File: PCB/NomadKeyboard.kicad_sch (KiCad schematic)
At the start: 93 parts, among them J1 4PIN, J2 OLED, P1 i2c_pin, P2 i2c_pin, SW1 SW_PUSH_LED, SW10 SW_PUSH_LED, SW11 SW_PUSH_LED, SW12 SW_PUSH_LED, SW13 SW_PUSH_LED, SW14 SW_PUSH_LED, SW15 SW_PUSH_LED, SW16 SW_PUSH_LED, SW17 SW_PUSH_LED, SW18 SW_PUSH_LED, SW19 SW_PUSH_LED, SW2 SW_PUSH_LED, SW20 SW_PUSH_LED, SW21 SW_PUSH_LED, SW22 SW_PUSH_LED, SW23 SW_PUSH_LED, SW24 SW_PUSH_LED, SW25 SW_PUSH_LED, SW26 SW_PUSH_LED, SW27 SW_PUSH_LED, SW28 SW_PUSH_LED, SW29 SW_PUSH_LED, SW3 SW_PUSH_LED, SW30 SW_PUSH_LED, SW31 SW_PUSH_LED, SW32 SW_PUSH_LED, SW33 SW_PUSH_LED, SW34 SW_PUSH_LED, SW4 SW_PUSH_LED, SW5 SW_PUSH_LED, SW6 SW_PUSH_LED, SW7 SW_PUSH_LED, SW8 SW_PUSH_LED, SW9 SW_PUSH_LED, U1 ProMicro

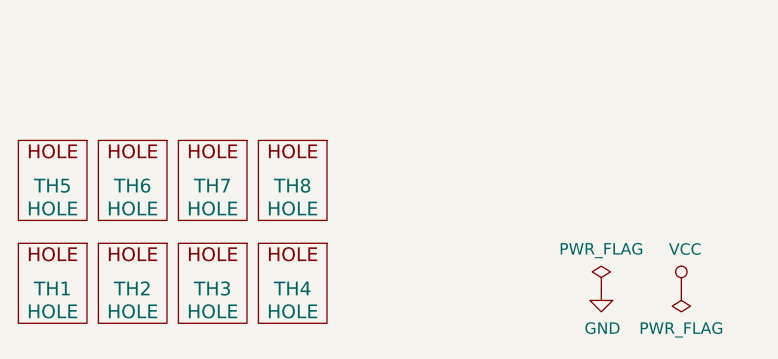
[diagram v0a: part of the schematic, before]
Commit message: Additional mounting hole, Logo and QR Code on Silkscreen
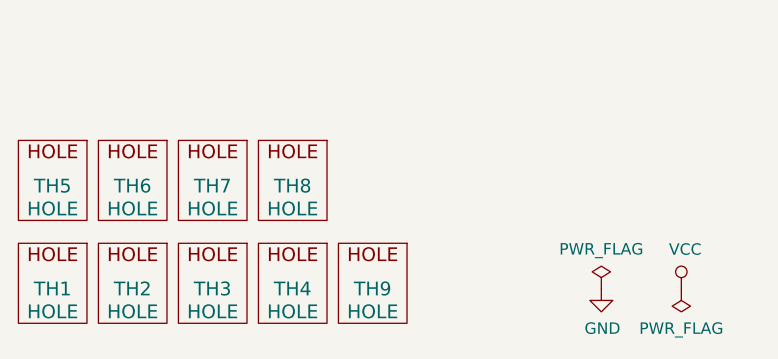
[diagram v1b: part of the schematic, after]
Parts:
- added TH9: HOLE, SofleChoc:HOLE_M2_TH, symbol SofleKeyboard-rescue:HOLE-Lily58-cache-Lily58_Pro-rescue
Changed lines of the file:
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@@
+	)
+	(symbol
+		(lib_id "SofleKeyboard-rescue:HOLE-Lily58-cache-Lily58_Pro-rescue")
+		(at 55.88 190.5 0)
+		(unit 1)
+		(exclude_from_sim no)
+		(in_bom yes)
+		(on_board yes)
+		(dnp no)
+		(property "Reference" "TH9"
+			(at 55.88 190.5 0)
+			(effects
+				(font
+					(size 1.524 1.524)
+				)
+			)
+		)
+		(property "Value" "HOLE"
+			(at 55.88 193.04 0)
+			(effects
+				(font
+					(size 1.524 1.524)
+				)
+			)
+		)
+		(property "Footprint" "SofleChoc:HOLE_M2_TH"
+			(at 55.88 190.5 0)
+			(effects
+				(font
+					(size 1.524 1.524)
+				)
+				(hide yes)
+			)
+		)
+		(property "Datasheet" ""
+			(at 55.88 190.5 0)
+			(effects
+				(font
+					(size 1.524 1.524)
+				)
+			)
+		)
+		(property "Description" ""
+			(at 55.88 190.5 0)
+			(effects
+				(font
+					(size 1.27 1.27)
+				)
+				(hide yes)
+			)
+		)
+		(instances
+			(project "NomadKeyboard"
+				(path "/eaee3b4b-85c3-461f-869e-93e0a5fc0df7"
+					(reference "TH9")
+					(unit 1)
+				)
+			)
+		)
 	)
 	(symbol
